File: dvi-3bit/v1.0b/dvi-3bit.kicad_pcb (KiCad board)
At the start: 4 copper layers, 37 x 20.3 mm, 32 parts, among them J1 PMOD, J2 jmp, J3 5V, J4 3v3_5v_sel, J5 HDMI_A_1.4, U1 VREG_3V3, U2 TFP410

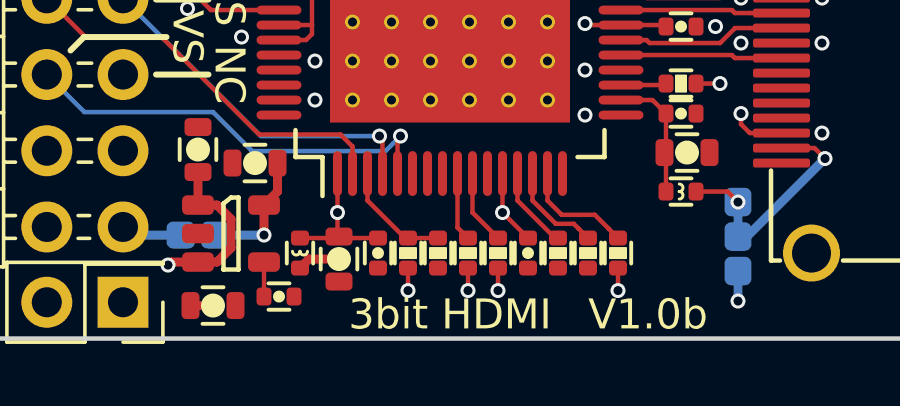
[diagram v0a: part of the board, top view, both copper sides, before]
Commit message: A few minor fixes to the dvi PMODs.
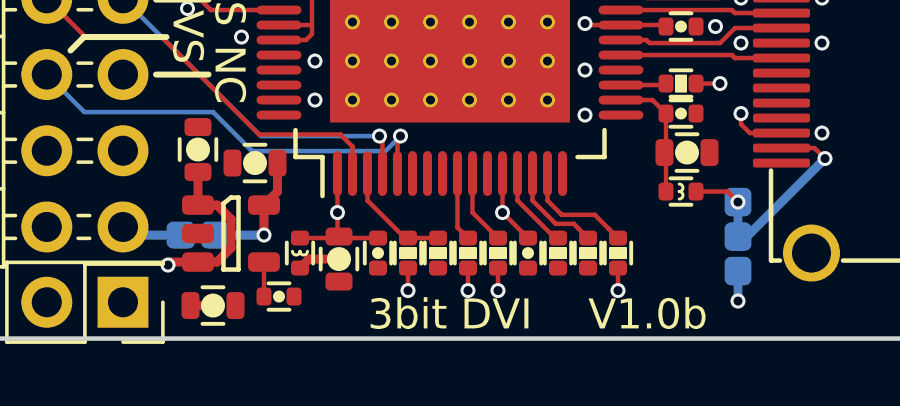
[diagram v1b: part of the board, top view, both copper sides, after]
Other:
- board text added: "3bit DVI"
- board text removed: "3bit HDMI"
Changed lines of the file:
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@@
   )
   (setup
-    (last_trace_width 0.3)
+    (last_trace_width 0.15)
     (user_trace_width 0.2)
     (user_trace_width 0.25)
@@
   (gr_arc (start 31 49.3) (end 30 49.3) (angle -90) (layer Edge.Cuts) (width 0.15))
   (gr_arc (start 66 49.3) (end 66 50.3) (angle -90) (layer Edge.Cuts) (width 0.15))
-  (gr_text "3bit HDMI" (at 47.5 49.5) (layer F.SilkS)
+  (gr_text "3bit DVI" (at 47.5 49.5) (layer F.SilkS)
     (effects (font (size 1 1) (thickness 0.2)))
   )

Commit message: Added pdf schematic exports to all projects plus minor fixes.
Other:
- board text added: "1BitSquared 2019"
- board text removed: "1BitSquared 2018"
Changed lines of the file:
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@@
     (rev V1.0b)
     (company 1BitSquared)
-    (comment 1 "(C) 2018 Piotr Esden-Tempski <piotr@esden.net>")
-    (comment 2 "(C) 2018 1BitSquared <info@1bitsquared.com>")
+    (comment 1 "(C) 2018-2019 Piotr Esden-Tempski <piotr@esden.net>")
+    (comment 2 "(C) 2018-2019 1BitSquared <info@1bitsquared.com>")
     (comment 3 "License: CC-BY-SA V4.0")
   )
@@
     (effects (font (size 1 1) (thickness 0.25)) (justify mirror))
   )
-  (gr_text "1BitSquared 2018" (at 55.35 40.2 270) (layer B.SilkS)
+  (gr_text "1BitSquared 2019" (at 55.35 40.2 270) (layer B.SilkS)
     (effects (font (size 1 1) (thickness 0.2)) (justify mirror))
   )

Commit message: Some global cleanup.
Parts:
- added REF**: null_Logo_SilkS_7.5mm, pkl_logos:null_Logo_SilkS_7.5mm, B.Cu at (47.5, 40.2)
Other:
- board text added: "NULL"
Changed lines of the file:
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@@
-(kicad_pcb (version 20171130) (host pcbnew 5.0.2-bee76a0~70~ubuntu18.04.1)
+(kicad_pcb (version 20171130) (host pcbnew 5.1.5-52549c5~86~ubuntu19.10.1)
   (general
     (thickness 1.6)
-    (drawings 49)
+    (drawings 50)
     (tracks 269)
     (zones 0)
-    (modules 32)
+    (modules 33)
     (nets 44)
   )
@@
     (zone_45_only no)
     (trace_min 0.15)
-    (segment_width 0.2)
-    (edge_width 0.15)
     (via_size 0.5)
     (via_drill 0.3)
@@
     (uvia_min_size 0.2)
     (uvia_min_drill 0.1)
+    (edge_width 0.15)
+    (segment_width 0.2)
     (pcb_text_width 0.3)
     (pcb_text_size 1.5 1.5)
@@
     (add_net "Net-(U2-Pad7)")
     (add_net "Net-(U2-Pad8)")
+  )
+  (module pkl_logos:null_Logo_SilkS_7.5mm (layer B.Cu)
+    (at 47.5 40.2 90)
+    (fp_text reference REF** (at 0 -5 90) (layer B.Fab)
+      (effects (font (size 1 1) (thickness 0.15)) (justify mirror))
+    )
+    (fp_text value null_Logo_SilkS_7.5mm (at 0 5 90) (layer B.Fab)
+      (effects (font (size 1 1) (thickness 0.15)) (justify mirror))
+    )
+    (fp_line (start 1 -0.5) (end 1.5 -0.5) (layer B.SilkS) (width 0.15))
+    (fp_line (start 1 0.5) (end 1 -0.5) (layer B.SilkS) (width 0.15))
+    (fp_line (start 0.2 -0.5) (end 0.7 -0.5) (layer B.SilkS) (width 0.15))
+    (fp_line (start 0.2 0.5) (end 0.2 -0.5) (layer B.SilkS) (width 0.15))
+    (fp_line (start -0.1 -0.2) (end -0.1 0.5) (layer B.SilkS) (width 0.15))
+    (fp_arc (start -0.4 -0.2) (end -0.7 -0.2) (angle 180) (layer B.SilkS) (width 0.15))
+    (fp_line (start -0.7 0.5) (end -0.7 -0.2) (layer B.SilkS) (width 0.15))
+    (fp_line (start -1 -0.5) (end -1 0.5) (layer B.SilkS) (width 0.15))
+    (fp_line (start -1.5 0.5) (end -1 -0.5) (layer B.SilkS) (width 0.15))
+    (fp_line (start -1.5 -0.5) (end -1.5 0.5) (layer B.SilkS) (width 0.15))
+    (fp_line (start 3.75 3.75) (end -3.75 3.75) (layer B.SilkS) (width 0.3))
+    (fp_line (start -3.75 3.75) (end -3.75 -3.75) (layer B.SilkS) (width 0.3))
+    (fp_line (start 3.75 3.75) (end 3.75 -3.75) (layer B.SilkS) (width 0.3))
+    (fp_line (start -3.75 -3.75) (end 3.75 -3.75) (layer B.SilkS) (width 0.3))
   )
   (module pkl_jumpers:J_NCNO_0903_30 (layer B.Cu)
@@
     )
   )
+  (gr_text NULL (at 42.8 40.3 270) (layer B.SilkS)
+    (effects (font (size 1 1) (thickness 0.2)) (justify mirror))
+  )
   (gr_text 3V3 (at 31.6 46.55) (layer B.SilkS)
